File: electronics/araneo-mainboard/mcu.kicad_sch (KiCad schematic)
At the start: 21 parts, among them J9 GPIO, SW2 BUTTON, SW3 RESET

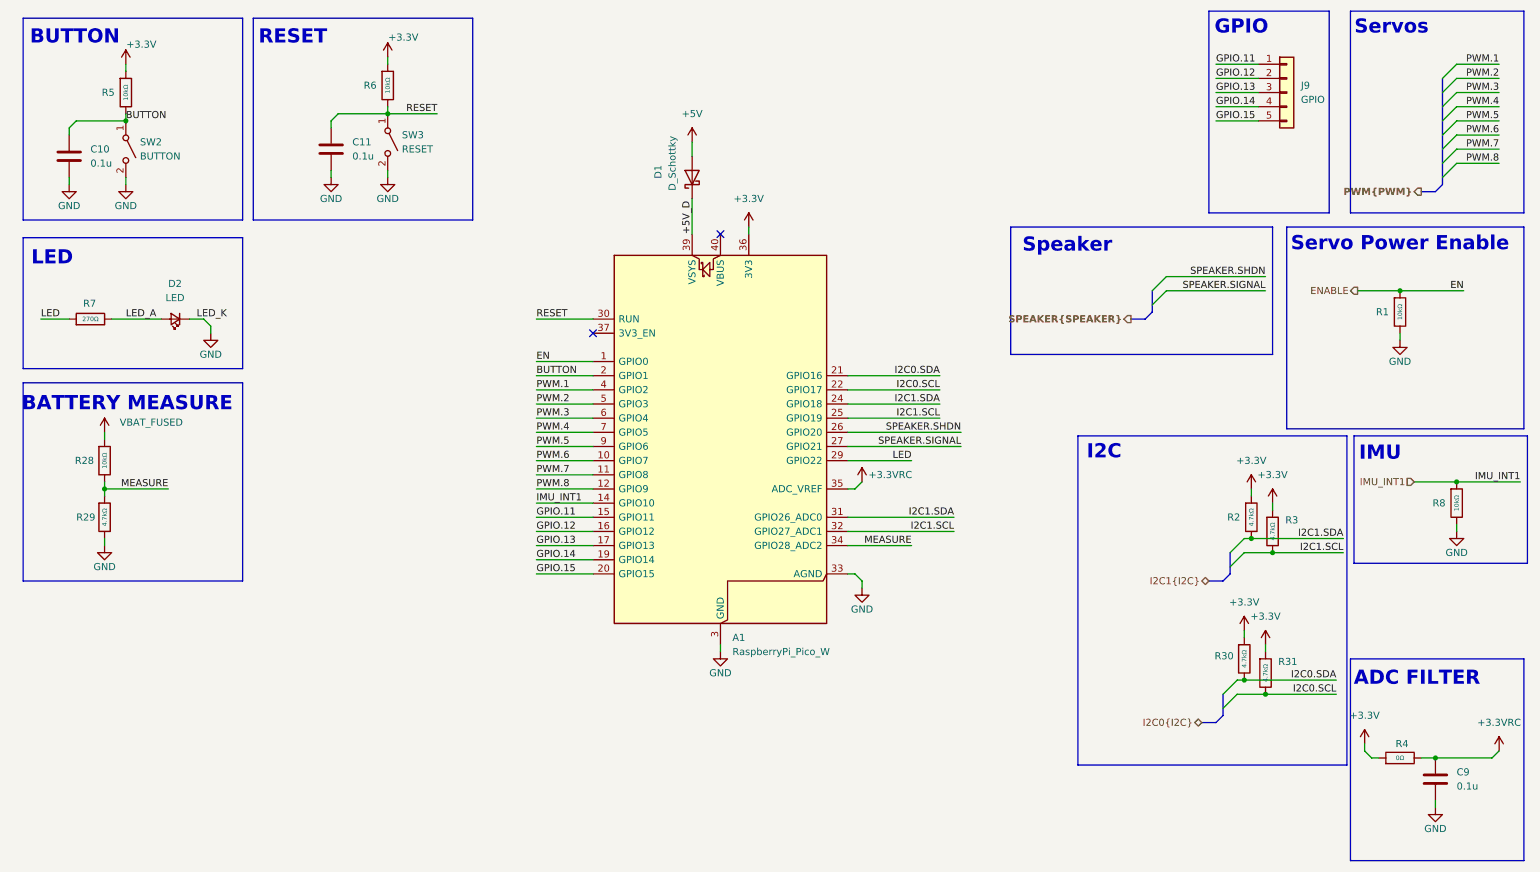
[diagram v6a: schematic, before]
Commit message: improve schematic and layout, add LCSC parts
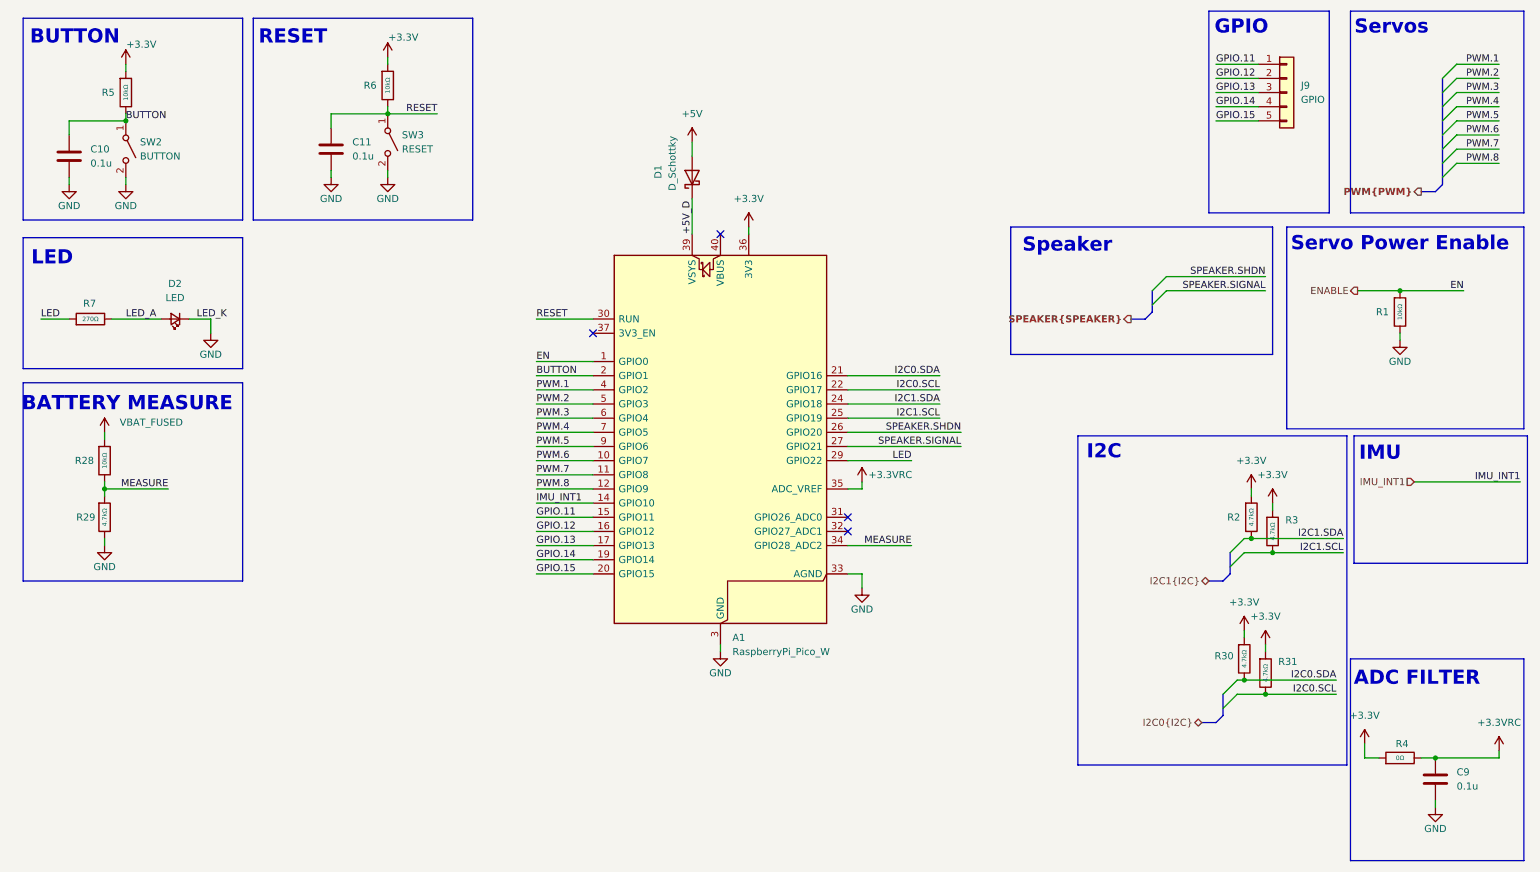
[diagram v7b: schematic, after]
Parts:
- removed R8: 10kΩ, PCM_JLCPCB:R_0402, symbol PCM_JLCPCB-Resistors:0402,1.2kΩ
- D1: footprint PCM_JLCPCB:D_0603 -> PCM_SparkFun-Semiconductor-Standard:SOD-123
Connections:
- net I2C1.SCL: no longer A1.32 (GPIO27_ADC1)
- net I2C1.SDA: no longer A1.31 (GPIO26_ADC0)
- no-connect marks 2 -> 4
